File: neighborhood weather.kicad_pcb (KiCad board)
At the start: 2 copper layers, 2 parts

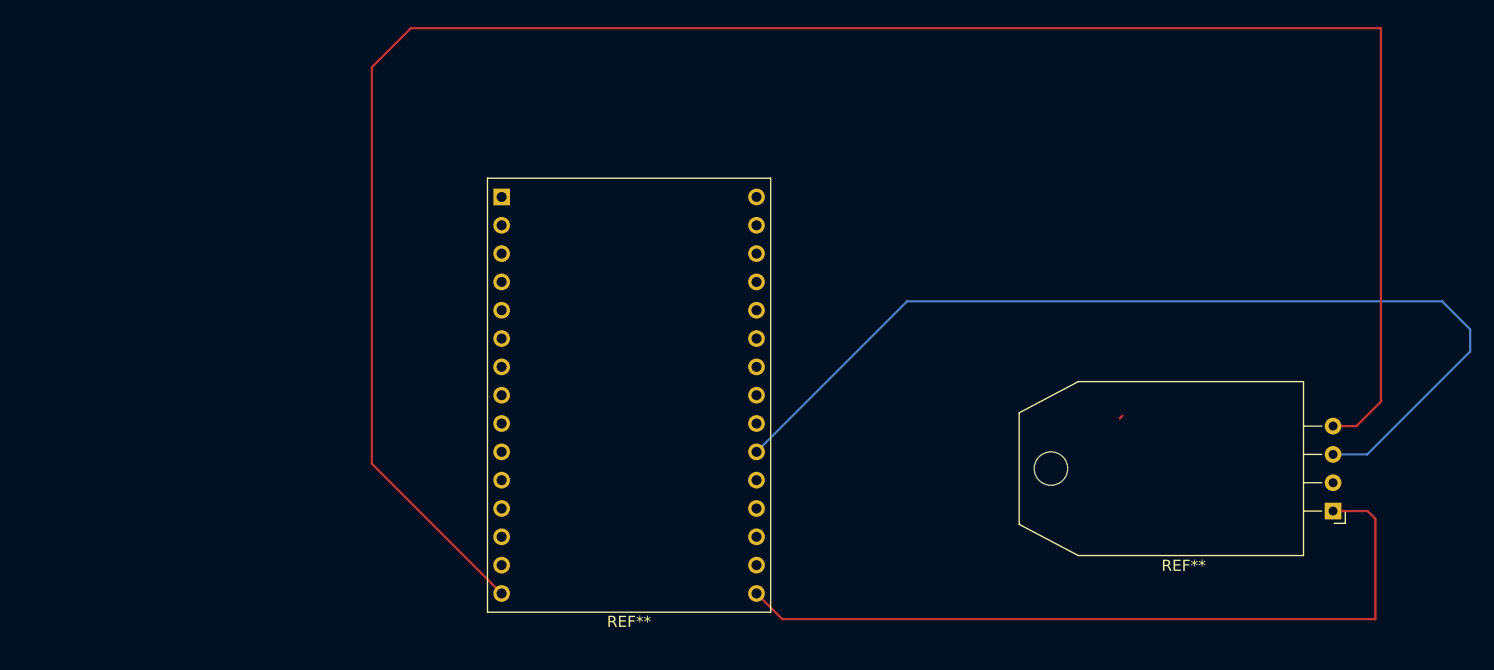
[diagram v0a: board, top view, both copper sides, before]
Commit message: added an anemometer symbol, rewired everything+changed board
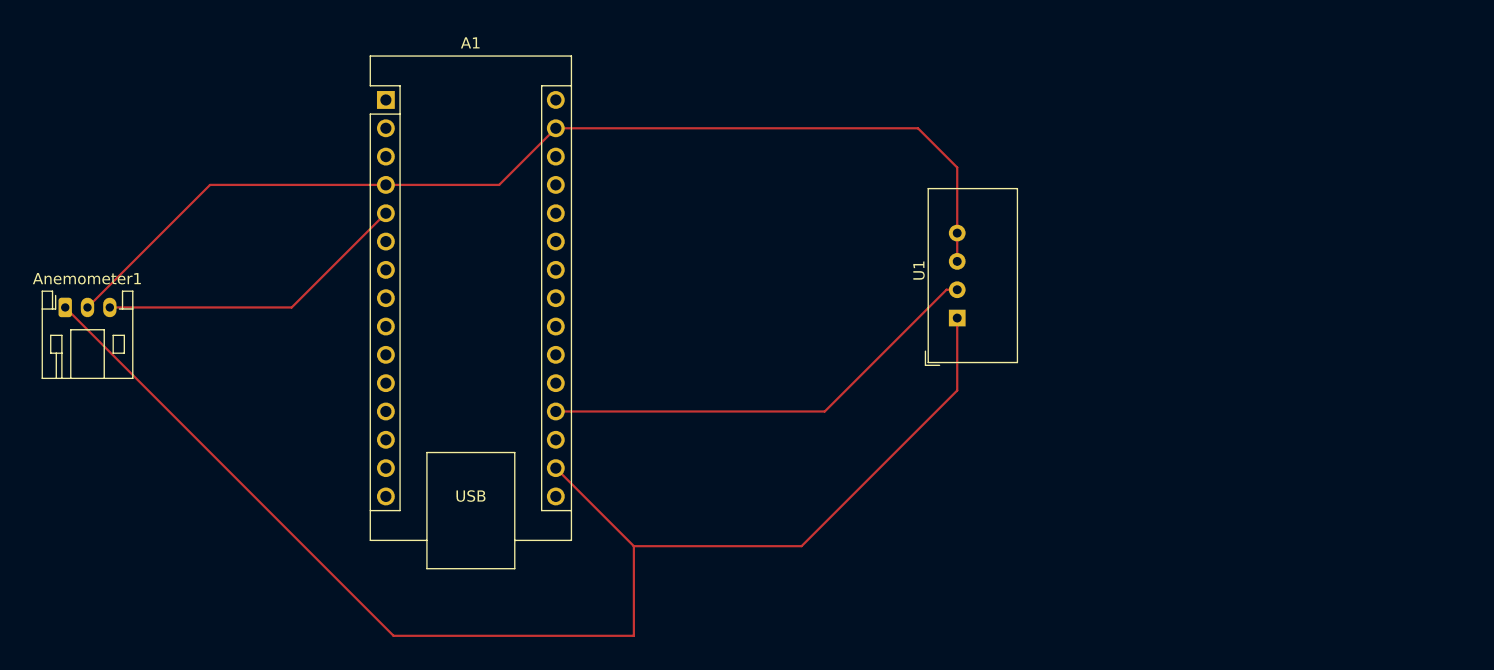
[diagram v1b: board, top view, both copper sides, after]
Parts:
- removed REF**: ESP32-C3-DevKitM-1, RF_Module:ESP32-C3-DevKitM-1
- removed REF**: ASAIR_AM2302_P2.54mm_Lead2.75mm_TabDown, Sensor:ASAIR_AM2302_P2.54mm_Lead2.75mm_TabDown
- added A1: Arduino_Nano_ESP32, Module:Arduino_Nano, F.Cu at (119.3, 64.9)
- added Anemometer1: ~, Connector_JST:JST_PH_S3B-PH-K_1x03_P2.00mm_Horizontal, F.Cu at (90.5, 83.5)
- added U1: AM2302, Sensor:ASAIR_AM2302_P2.54mm_Vertical, F.Cu at (170.5, 84.5)
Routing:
- net (no net): track 341.3 -> 0.00 mm
- net Net-(A1-3V3): track 0.00 -> 122.4 mm
- net Net-(Anemometer1-GND): track 0.00 -> 94.5 mm
- net Net-(A1-A0): track 0.00 -> 40.5 mm
- net Net-(A1-D2): track 0.00 -> 28.3 mm

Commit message: board outline added and anemometer finished
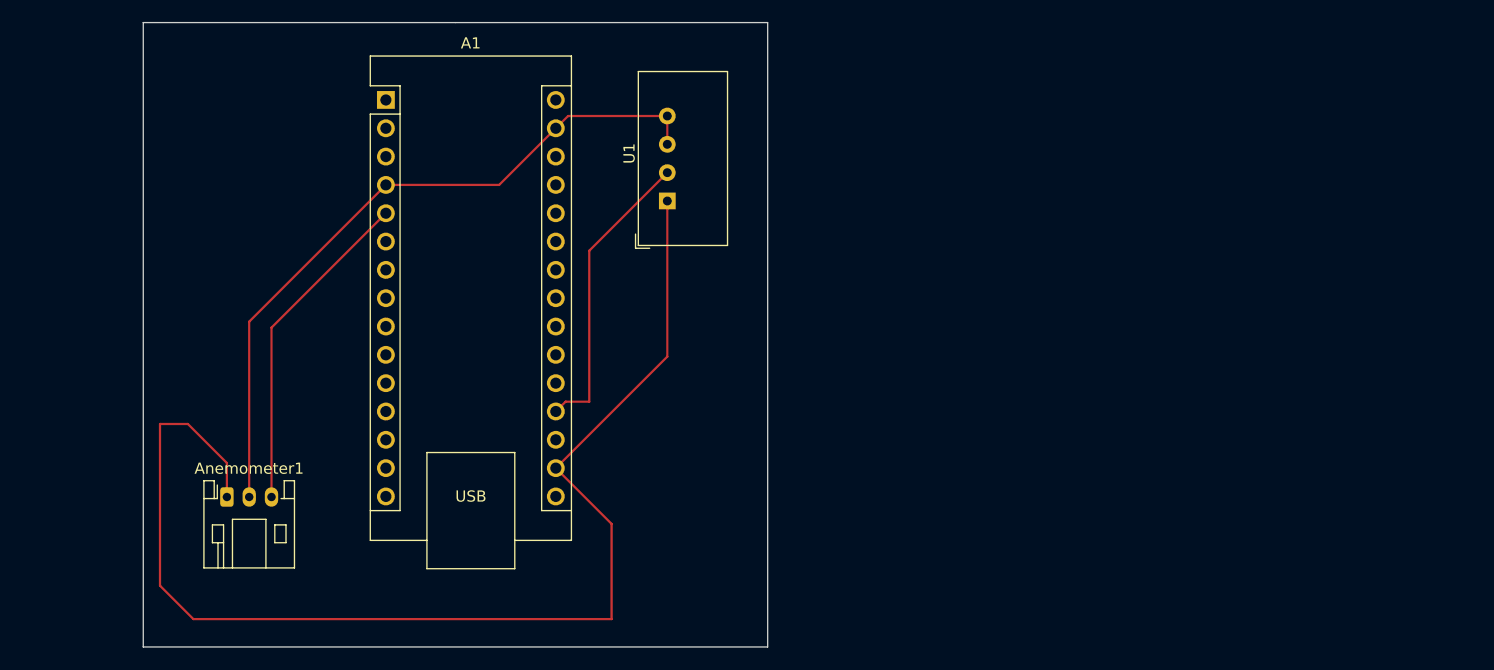
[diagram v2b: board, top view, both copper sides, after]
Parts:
- moved U1 28.0 mm to (144.5, 74.0)
- moved Anemometer1 22.3 mm to (105.0, 100.5)
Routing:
- net Net-(Anemometer1-GND): track 94.5 -> 63.4 mm
- net Net-(A1-A0): track 40.5 -> 26.8 mm
- net Net-(A1-3V3): track 122.4 -> 110.5 mm
- net Net-(A1-D2): track 28.3 -> 29.7 mm
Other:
- board outline added: 56 x 56 mm
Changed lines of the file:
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@@
 	(footprint "Connector_JST:JST_PH_S3B-PH-K_1x03_P2.00mm_Horizontal"
 		(layer "F.Cu")
-		(at 90.5 83.55)
+		(at 105 100.55)
 		(descr "JST PH series connector, S3B-PH-K (http://www.jst-mfg.com/product/pdf/eng/ePH.pdf), generated with kicad-footprint-generator")
 		(tags "connector JST PH horizontal")
@@
 	(footprint "Sensor:ASAIR_AM2302_P2.54mm_Vertical"
 		(layer "F.Cu")
-		(at 170.5 84.5 90)
+		(at 144.5 74 90)
 		(descr "Temperature and humidity module, http://akizukidenshi.com/download/ds/aosong/AM2302.pdf")
 		(tags "Temperature and humidity module DHT22 AM2302")
@@
 		)
 	)
-	(segment
-		(start 141.5 113)
-		(end 141.5 104.96)
+	(gr_line
+		(start 97.5 114)
+		(end 153.5 114)
+		(stroke
+			(width 0.05)
+			(type default)
+		)
+		(layer "Edge.Cuts")
+	)
+	(gr_line
+		(start 97.5 58)
+		(end 97.5 114)
+		(stroke
+			(width 0.05)
+			(type default)
+		)
+		(layer "Edge.Cuts")
+	)
+	(gr_line
+		(start 153.5 114)
+		(end 153.5 58)
+		(stroke
+			(width 0.05)
+			(type default)
+		)
+		(layer "Edge.Cuts")
+	)
+	(gr_line
+		(start 153.5 58)
+		(end 125.5 58)
+		(stroke
+			(width 0.05)
+			(type default)
+		)
+		(layer "Edge.Cuts")
+	)
+	(gr_line
+		(start 125.5 58)
+		(end 97.5 58)
+		(stroke
+			(width 0.05)
+			(type default)
+		)
+		(layer "Edge.Cuts")
+	)
+	(segment
+		(start 144.5 74)
+		(end 144.5 87.96)
 		(width 0.2)
 		(layer "F.Cu")
@@
 	)
 	(segment
-		(start 156.54 104.96)
-		(end 141.5 104.96)
+		(start 105 97.5)
+		(end 101.5 94)
 		(width 0.2)
 		(layer "F.Cu")
@@
 	)
 	(segment
-		(start 119.95 113)
-		(end 141.5 113)
+		(start 102 111.5)
+		(end 139.5 111.5)
 		(width 0.2)
 		(layer "F.Cu")
@@
 	)
 	(segment
-		(start 141.5 104.96)
+		(start 99 108.5)
+		(end 102 111.5)
+		(width 0.2)
+		(layer "F.Cu")
+		(net 26)
+	)
+	(segment
+		(start 105 100.55)
+		(end 105 97.5)
+		(width 0.2)
+		(layer "F.Cu")
+		(net 26)
+	)
+	(segment
+		(start 144.5 87.96)
 		(end 134.5 97.96)
 		(width 0.2)
@@
 	)
 	(segment
-		(start 170.5 84.5)
-		(end 170.5 91)
+		(start 139.5 111.5)
+		(end 139.5 102.96)
 		(width 0.2)
 		(layer "F.Cu")
@@
 	)
 	(segment
-		(start 170.5 91)
-		(end 156.54 104.96)
+		(start 139.5 102.96)
+		(end 134.5 97.96)
 		(width 0.2)
 		(layer "F.Cu")
@@
 	)
 	(segment
-		(start 90.5 83.55)
-		(end 119.95 113)
+		(start 99 94)
+		(end 99 108.5)
 		(width 0.2)
 		(layer "F.Cu")
@@
 	)
 	(segment
-		(start 170.5 81.96)
-		(end 169.54 81.96)
+		(start 101.5 94)
+		(end 99 94)
+		(width 0.2)
+		(layer "F.Cu")
+		(net 26)
+	)
+	(segment
+		(start 137.5 92)
+		(end 135.38 92)
 		(width 0.2)
 		(layer "F.Cu")
@@
 	)
 	(segment
-		(start 169.54 81.96)
-		(end 158.62 92.88)
+		(start 137.5 78.46)
+		(end 137.5 92)
 		(width 0.2)
 		(layer "F.Cu")
@@
 	)
 	(segment
-		(start 158.62 92.88)
+		(start 144.5 71.46)
+		(end 137.5 78.46)
+		(width 0.2)
+		(layer "F.Cu")
+		(net 27)
+	)
+	(segment
+		(start 135.38 92)
 		(end 134.5 92.88)
 		(width 0.2)
@@
 	)
 	(segment
-		(start 103.49 72.56)
+		(start 144.5 68.92)
+		(end 144.5 66.38)
+		(width 0.2)
+		(layer "F.Cu")
+		(net 28)
+	)
+	(segment
+		(start 144.5 66.38)
+		(end 135.6 66.38)
+		(width 0.2)
+		(layer "F.Cu")
+		(net 28)
+	)
+	(segment
+		(start 129.42 72.56)
+		(end 134.5 67.48)
+		(width 0.2)
+		(layer "F.Cu")
+		(net 28)
+	)
+	(segment
+		(start 135.6 66.38)
+		(end 134.5 67.48)
+		(width 0.2)
+		(layer "F.Cu")
+		(net 28)
+	)
+	(segment
+		(start 119.26 72.56)
+		(end 129.42 72.56)
+		(width 0.2)
+		(layer "F.Cu")
+		(net 28)
+	)
+	(segment
+		(start 107 100.55)
+		(end 107 84.82)
+		(width 0.2)
+		(layer "F.Cu")
+		(net 28)
+	)
+	(segment
+		(start 107 84.82)
 		(end 119.26 72.56)
 		(width 0.2)
@@
 	)
 	(segment
-		(start 166.98 67.48)
-		(end 134.5 67.48)
-		(width 0.2)
-		(layer "F.Cu")
-		(net 28)
-	)
-	(segment
-		(start 170.5 76.88)
-		(end 170.5 71)
-		(width 0.2)
-		(layer "F.Cu")
-		(net 28)
-	)
-	(segment
-		(start 129.42 72.56)
-		(end 119.26 72.56)
-		(width 0.2)
-		(layer "F.Cu")
-		(net 28)
-	)
-	(segment
-		(start 92.5 83.55)
-		(end 103.49 72.56)
-		(width 0.2)
-		(layer "F.Cu")
-		(net 28)
-	)
-	(segment
-		(start 170.5 71)
-		(end 166.98 67.48)
-		(width 0.2)
-		(layer "F.Cu")
-		(net 28)
-	)
-	(segment
-		(start 170.5 79.42)
-		(end 170.5 76.88)
-		(width 0.2)
-		(layer "F.Cu")
-		(net 28)
-	)
-	(segment
-		(start 134.5 67.48)
-		(end 129.42 72.56)
-		(width 0.2)
-		(layer "F.Cu")
-		(net 28)
-	)
-	(segment
-		(start 94.5 83.55)
-		(end 110.81 83.55)
+		(start 109 85.36)
+		(end 119.26 75.1)
 		(width 0.2)
 		(layer "F.Cu")
@@
 	)
 	(segment
-		(start 110.81 83.55)
-		(end 119.26 75.1)
-		(width 0.2)
-		(layer "F.Cu")
+		(start 109 100.55)
+		(end 109 85.36)
+		(width 0.2)
+		(layer "F.Cu")
